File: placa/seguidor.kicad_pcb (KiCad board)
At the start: 2 copper layers, 51 x 58 mm, 25 parts, among them J1 conn_bat, J2 conn_sensores, J3 conn_motor, J4 conn_pwm, J5 conn_icsp, SW1 SW_custom, SW2 btn_arranque, U1 ATmega328P-P, U2 LM7805_TO220, Y1 Crystal

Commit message: esquemático del diseño nuevo de la placa, falta el pcb
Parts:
- added C8: 100u, Capacitor_THT:CP_Radial_D5.0mm_P2.00mm, F.Cu at (30.7, 53.1)
- added C9: 100u, Capacitor_THT:CP_Radial_D5.0mm_P2.00mm, F.Cu at (30.7, 59.6)
- added D2: 1N4007, Diode_THT:D_DO-41_SOD81_P10.16mm_Horizontal, F.Cu at (33.5, 104.8)
- added D3: 1N4007, Diode_THT:D_DO-41_SOD81_P10.16mm_Horizontal, F.Cu at (33.5, 109.0)
- added J6: conn_bt, Connector_PinSocket_2.54mm:PinSocket_1x06_P2.54mm_Horizontal, F.Cu at (39.1, 76.5)
- added J7: jumper_bt, Connector_PinHeader_2.54mm:PinHeader_1x02_P2.54mm_Vertical, F.Cu at (37.3, 61.6)
- added R10: 3.3k, Resistor_THT:R_Axial_DIN0204_L3.6mm_D1.6mm_P5.08mm_Horizontal, F.Cu at (25.0, 126.3)
- added R11: 3.3k, Resistor_THT:R_Axial_DIN0204_L3.6mm_D1.6mm_P5.08mm_Horizontal, F.Cu at (25.0, 129.4)
- added R12: 3.3k, Resistor_THT:R_Axial_DIN0204_L3.6mm_D1.6mm_P5.08mm_Horizontal, F.Cu at (25.0, 132.6)
- added R13: 3.3k, Resistor_THT:R_Axial_DIN0204_L3.6mm_D1.6mm_P5.08mm_Horizontal, F.Cu at (36.5, 51.4)
- added R14: 3.3k, Resistor_THT:R_Axial_DIN0204_L3.6mm_D1.6mm_P5.08mm_Horizontal, F.Cu at (36.5, 54.5)
- added R15: 3.3k, Resistor_THT:R_Axial_DIN0204_L3.6mm_D1.6mm_P5.08mm_Horizontal, F.Cu at (36.5, 57.7)
- added R3: 3.3k, Resistor_THT:R_Axial_DIN0204_L3.6mm_D1.6mm_P5.08mm_Horizontal, F.Cu at (25.0, 104.2)
- added R4: 3.3k, Resistor_THT:R_Axial_DIN0204_L3.6mm_D1.6mm_P5.08mm_Horizontal, F.Cu at (25.0, 107.4)
- added R5: 3.3k, Resistor_THT:R_Axial_DIN0204_L3.6mm_D1.6mm_P5.08mm_Horizontal, F.Cu at (25.0, 110.5)
- added R6: 3.3k, Resistor_THT:R_Axial_DIN0204_L3.6mm_D1.6mm_P5.08mm_Horizontal, F.Cu at (25.0, 113.7)
- added R7: 3.3k, Resistor_THT:R_Axial_DIN0204_L3.6mm_D1.6mm_P5.08mm_Horizontal, F.Cu at (25.0, 116.8)
- added R8: 3.3k, Resistor_THT:R_Axial_DIN0204_L3.6mm_D1.6mm_P5.08mm_Horizontal, F.Cu at (25.0, 120.0)
- added R9: 3.3k, Resistor_THT:R_Axial_DIN0204_L3.6mm_D1.6mm_P5.08mm_Horizontal, F.Cu at (25.0, 123.1)
- J1: footprint Connector_Molex:Molex_KK-396_A-41791-0002_1x02_P3.96mm_Vertical -> Connector_PinHeader_2.54mm:PinHeader_1x02_P2.54mm_Vertical
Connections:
- net motor_izq renamed motor_izq1
- J4 pad 2: GND -> motor_izq2
- J4 pad 3: motor_der -> motor_der1
- J4 pad 4: GND -> motor_der2
- SW1 pad 1: VCC -> Net-(D2-A)
- U1 pad 12: motor_der -> motor_izq2
- U1 pad 13: unconnected-(U1-PD7-Pad13) -> state_bt
- U1 pad 15: boton_largada -> motor_der1
- U1 pad 16: led_arranque -> motor_der2
- U1 pad 2: unconnected-(U1-PD0-Pad2) -> txd_bt
- U1 pad 21: unconnected-(U1-AREF-Pad21) -> Net-(U1-AREF)
- U1 pad 27: unconnected-(U1-PC4-Pad27) -> sensor_bat
- U1 pad 3: unconnected-(U1-PD1-Pad3) -> rxd_bt
- U1 pad 4: unconnected-(U1-PD2-Pad4) -> boton_largada
- U1 pad 6: unconnected-(U1-PD4-Pad6) -> led_arranque
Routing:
- net motor_der: track 10.9 -> 0.00 mm
- net (no net): track 0.00 -> 10.9 mm

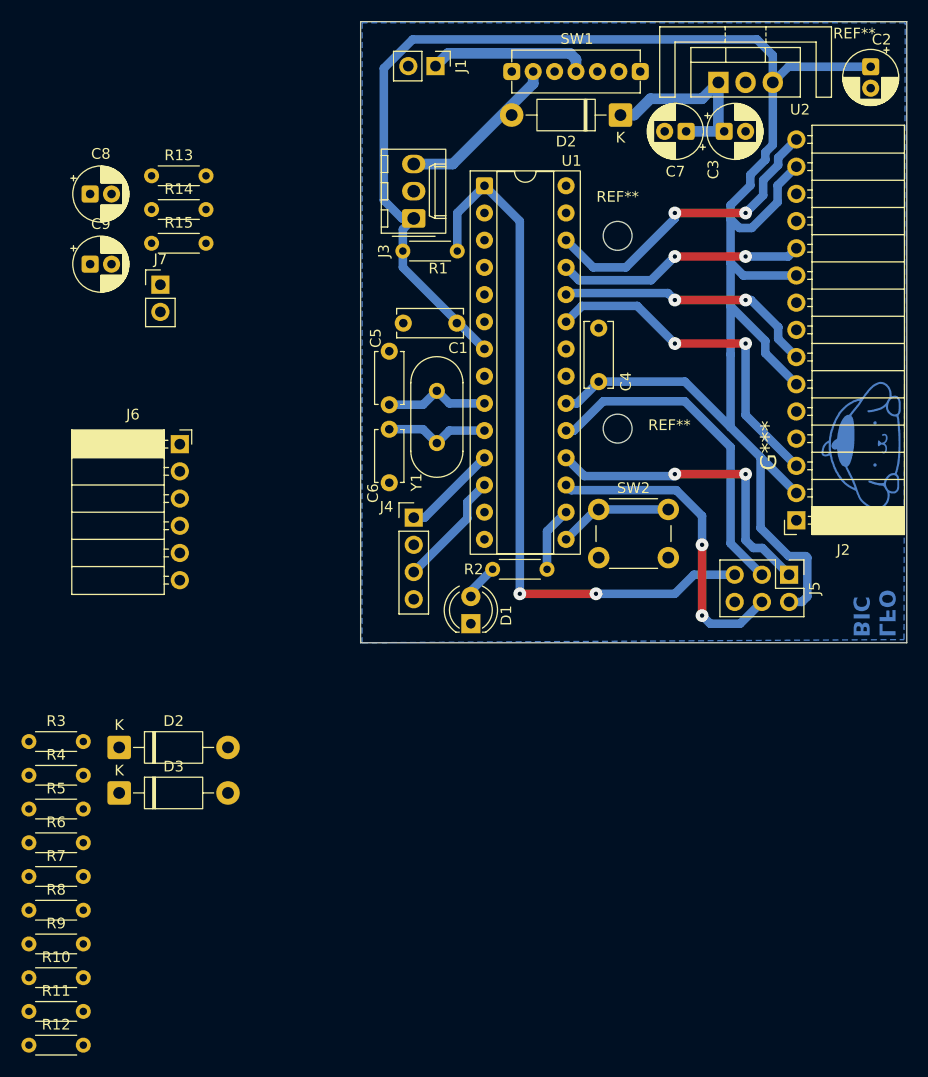
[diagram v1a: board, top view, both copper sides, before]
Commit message: diseño de placa con bluetooth y motores en reversa
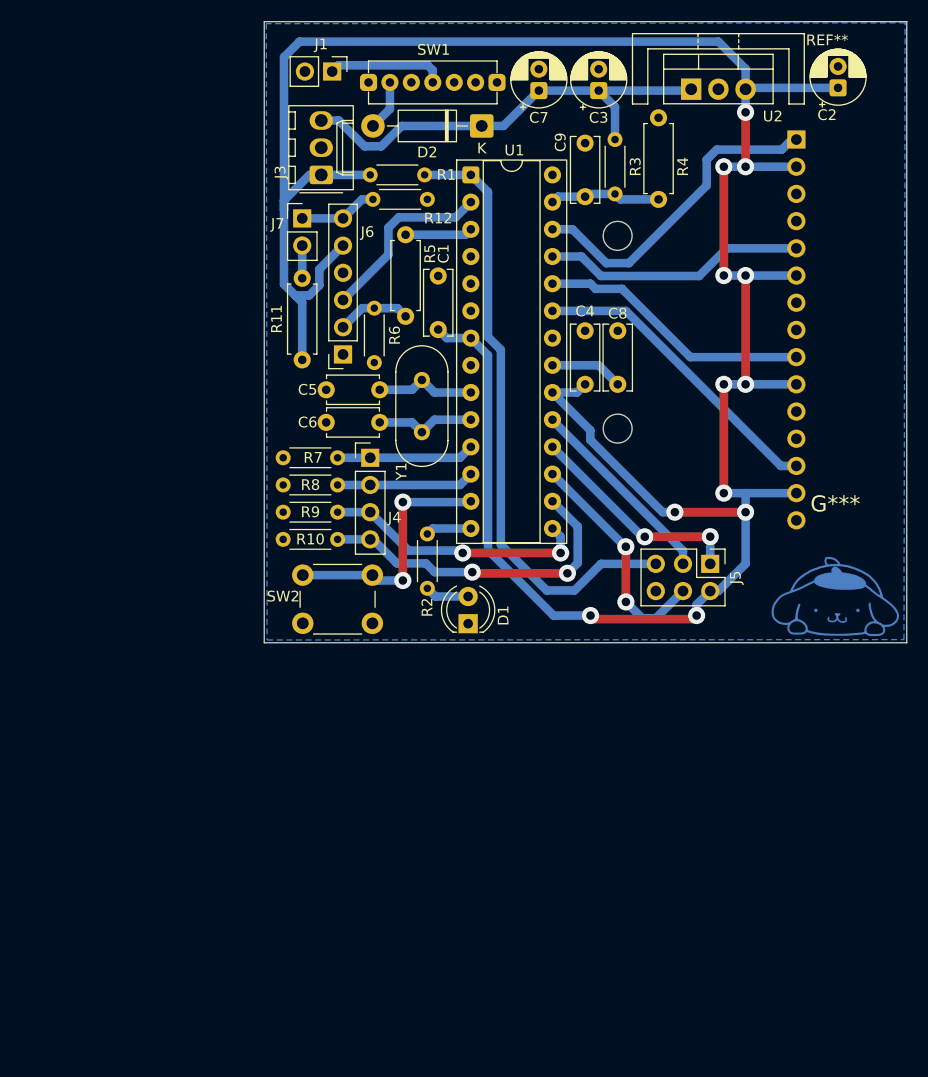
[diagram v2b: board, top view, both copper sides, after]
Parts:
- removed the D2 at (33.5, 104.8)
- removed the D2 at (80.3, 45.7)
- removed D3: 1N4007, Diode_THT:D_DO-41_SOD81_P10.16mm_Horizontal
- removed R13, R14, R15: 3.3k, Resistor_THT:R_Axial_DIN0204_L3.6mm_D1.6mm_P5.08mm_Horizontal
- added D2: 1N4007, Diode_THT:D_DO-41_SOD81_P10.16mm_Horizontal, F.Cu at (67.3, 46.7)
- C8, C9: value 100u -> 100n; footprint Capacitor_THT:CP_Radial_D5.0mm_P2.00mm -> Capacitor_THT:C_Disc_D6.0mm_W2.5mm_P5.00mm
- J2: moved to B.Cu
- J6: footprint Connector_PinSocket_2.54mm:PinSocket_1x06_P2.54mm_Horizontal -> Connector_PinSocket_2.54mm:PinSocket_1x06_P2.54mm_Vertical
- R11, R4, R5: value 3.3k -> 27k; footprint Resistor_THT:R_Axial_DIN0204_L3.6mm_D1.6mm_P5.08mm_Horizontal -> Resistor_THT:R_Axial_DIN0207_L6.3mm_D2.5mm_P7.62mm_Horizontal
- R12, R3, R6: value 3.3k -> 56k
- moved R12 87.3 mm to (62.2, 53.6), turned to 180 degrees
- moved R4 79.7 mm to (83.8, 53.6), turned to 90 degrees
- moved R3 78.5 mm to (79.8, 48.0), turned to -90 degrees
- moved R11 66.0 mm to (50.5, 68.6), turned to 90 degrees
- moved R5 64.1 mm to (60.2, 56.9), turned to -90 degrees
- moved R6 59.4 mm to (57.3, 63.8), turned to -90 degrees
- moved C8 52.4 mm to (80.0, 70.9), turned to 90 degrees
- moved R10 50.1 mm to (53.8, 85.3), turned to 180 degrees
- moved R9 49.6 mm to (53.8, 82.8), turned to 180 degrees
- moved R8 49.1 mm to (53.8, 80.3), turned to 180 degrees
- moved R7 48.6 mm to (53.8, 77.7), turned to 180 degrees
- moved C9 46.7 mm to (77.0, 53.3), turned to 90 degrees
- moved J2 35.6 mm to (96.7, 48.0)
- moved SW2 28.3 mm to (50.6, 88.7)
- moved J6 17.4 mm to (54.4, 68.1), turned to 180 degrees
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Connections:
- J2 pad 1: GND -> sensor1
- J2 pad 11: sensor2 -> GND
- J2 pad 13: GND -> sensor4
- J2 pad 15: sensor1 -> GND
- J2 pad 3: sensor4 -> GND
- J2 pad 5: GND -> sensor2
- J2 pad 7: sensor3 -> GND
- J2 pad 9: GND -> sensor3
- J3 pad 3: VCC -> V_IN
- J6 pad 1: state_bt -> unconnected-(J6-Pin_1-Pad1)
- R10 pad 1: motor_izq2 -> motor_der2
- R11 pad 1: motor_der1 -> +5V
- R11 pad 2: GND -> Net-(J7-Pin_2)
- R12 pad 1: motor_der2 -> GND
- R12 pad 2: GND -> key_bt
- R3 pad 1: VCC -> V_IN
- R3 pad 2: Net-(R3-Pad2) -> sensor_bat
- R4 pad 1: Net-(R3-Pad2) -> sensor_bat
- R4 pad 2: sensor_bat -> GND
- R5 pad 1: sensor_bat -> rxd_bt
- R5 pad 2: GND -> Net-(J6-Pin_2)
- R6 pad 1: rxd_bt -> Net-(J6-Pin_2)
- R6 pad 2: Net-(J6-Pin_2) -> GND
- R7 pad 1: Net-(J6-Pin_2) -> motor_izq1
- R7 pad 2: Net-(R7-Pad2) -> GND
- R8 pad 1: Net-(R7-Pad2) -> motor_izq2
- R9 pad 1: motor_izq1 -> motor_der1
- U1 pad 13: state_bt -> boton_largada
- U1 pad 14: unconnected-(U1-PB0-Pad14) -> led_arranque
- U1 pad 4: boton_largada -> unconnected-(U1-PD2-Pad4)
- U1 pad 6: led_arranque -> unconnected-(U1-PD4-Pad6)
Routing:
- net +5V: track 186.3 -> 253.1 mm, vias 0 -> 12
- net motor_der2: track 0.00 -> 30.9 mm, vias 0 -> 2
- net motor_der1: track 0.00 -> 25.0 mm, vias 0 -> 2
- net V_IN: track 18.8 -> 43.0 mm
- net txd_bt: track 0.00 -> 17.2 mm
- net VCC: track 15.4 -> 0.00 mm
- net sck: track 31.4 -> 18.5 mm
- net motor_izq2: track 0.00 -> 12.9 mm
- net boton_largada: track 10.7 -> 23.3 mm, vias 0 -> 2
- net (no net): track 10.9 -> 0.00 mm
- net sensor_bat: track 0.00 -> 10.4 mm
- net reset: track 67.4 -> 57.3 mm, vias 2 -> 0
- net miso: track 29.1 -> 20.8 mm
- net mosi: track 29.9 -> 21.8 mm
- net key_bt: track 0.00 -> 7.34 mm
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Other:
- board size 51 x 58 mm -> 60 x 58 mm
- board text removed: "LFO BIC"
